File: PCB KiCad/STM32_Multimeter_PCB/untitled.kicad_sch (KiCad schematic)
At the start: 51 parts, among them J10 Conn_01x02_Pin, J6 Barrel_Jack, J7 Conn_01x02_Pin, J8 Barrel_Jack, J9 Barrel_Jack, Q1 NMOS, Q2 NMOS, Q3 NMOS, Q4 NMOS, Q5 NMOS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

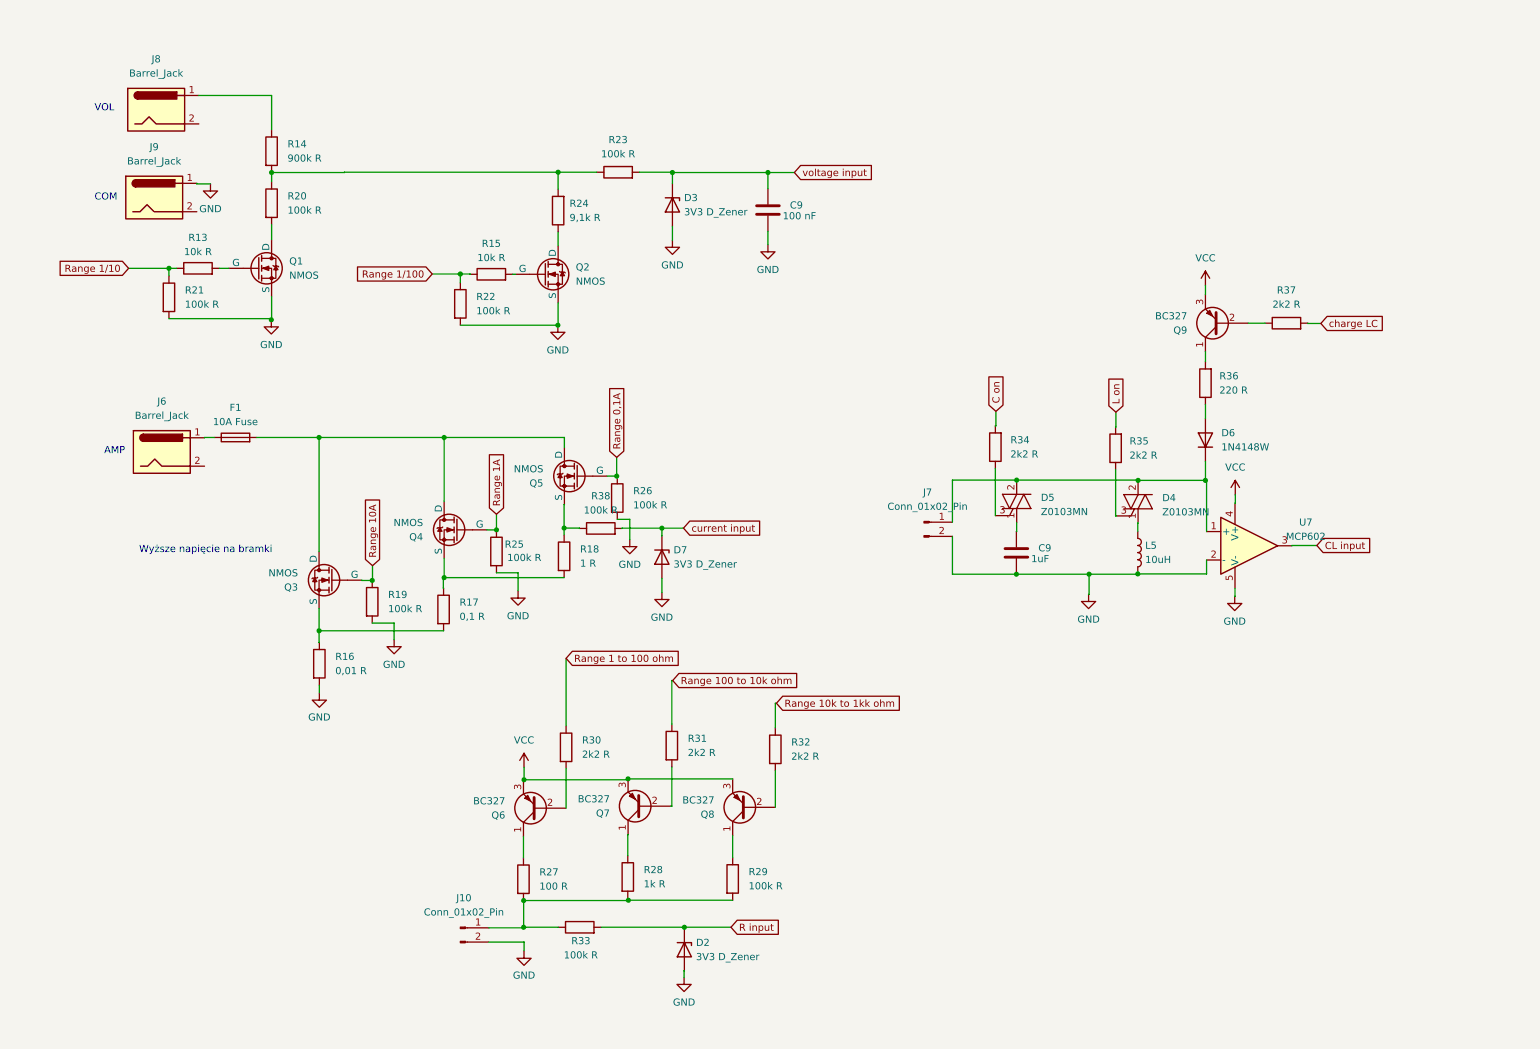
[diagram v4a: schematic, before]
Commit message: Added BJT for swiching range mosfets from 9V
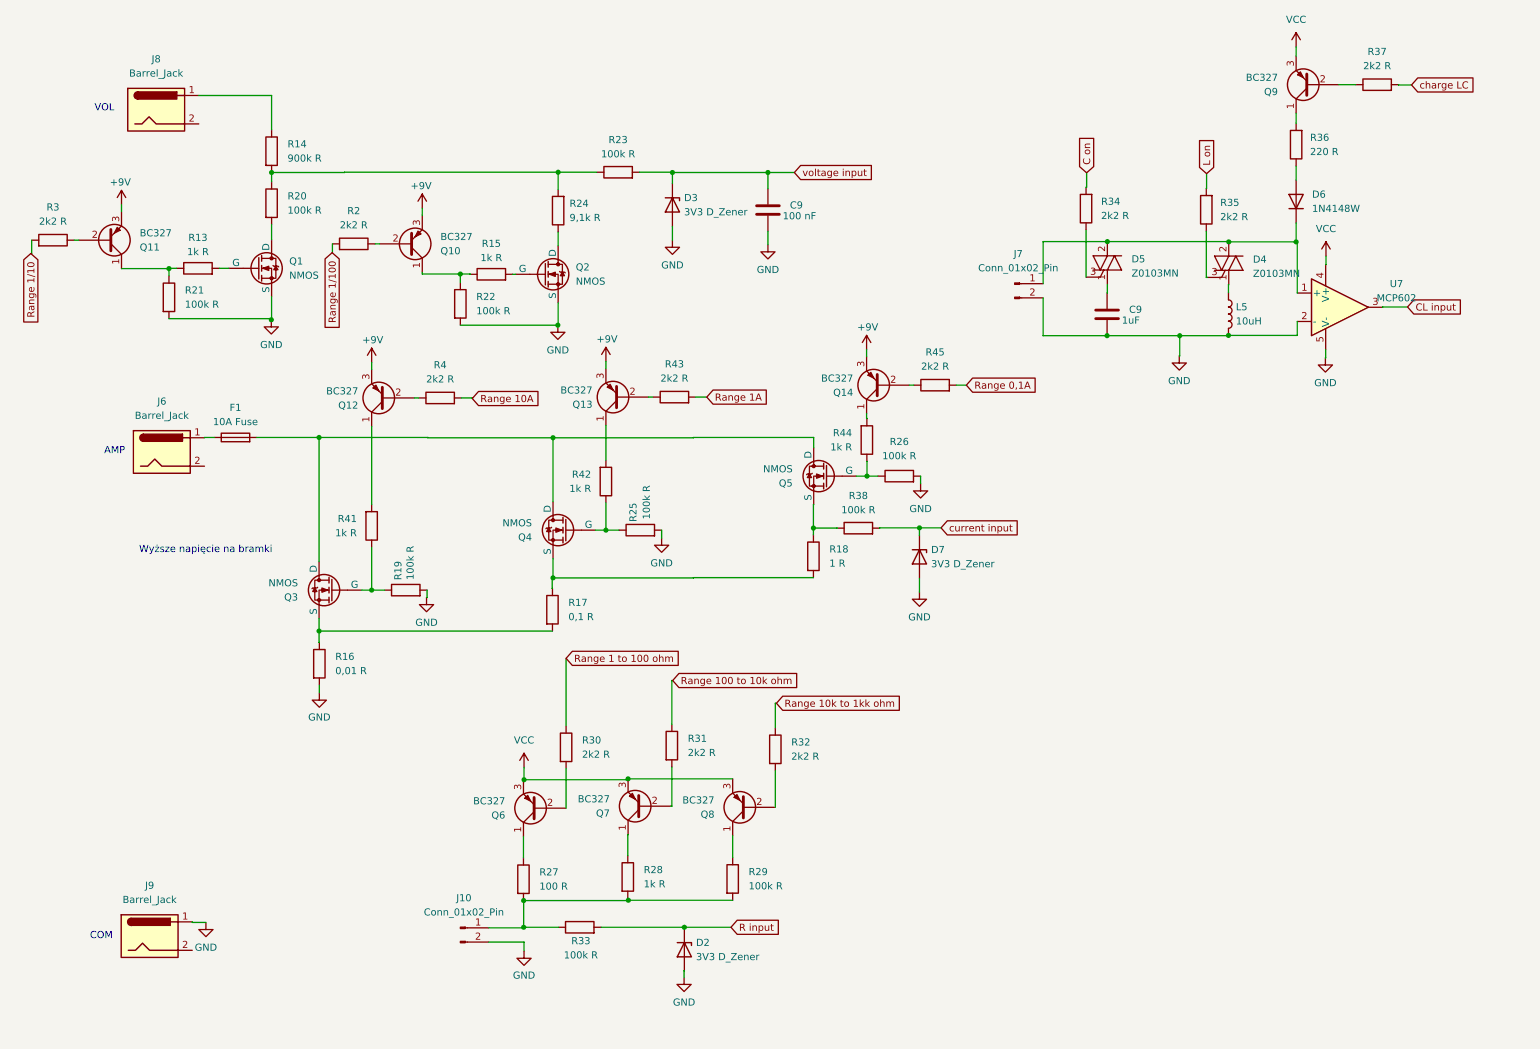
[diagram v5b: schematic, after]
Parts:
- added Q10, Q11, Q12, Q13, Q14: BC327, Package_TO_SOT_SMD:SOT-23-3, symbol Transistor_BJT:BC327
- added R2, R3, R4, R43, R45: 2k2 R, Resistor_SMD:R_0805_2012Metric, symbol Device:R
- added R41, R42, R44: 1k R, Resistor_SMD:R_0805_2012Metric, symbol Device:R
- R13, R15: value 10k R -> 1k R
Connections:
- net Range 0,1A: now also R45.2; no longer Q5.2 (G), R26.1
- net Range 10A: now also R4.2; no longer Q3.2 (G), R19.1
- net Range 1A: now also R43.2; no longer Q4.2 (G), R25.1
- net Range 1/10: now also R3.2; no longer R13.1, R21.1
- net Range 1/100: now also R2.2; no longer R15.1, R22.1
- new net: Q12.1 (C), R41.2
- new net: Q12.2 (B), R4.1
- new net: Q4.2 (G), R25.1, R42.1
- new net: Q11.1 (C), R13.1, R21.1
- new net: Q11.2 (B), R3.1
- new net: Q13.2 (B), R43.1
- new net: Q14.2 (B), R45.1
- new net: Q14.1 (C), R44.2
- new net: Q3.2 (G), R19.1, R41.1
- new net: Q13.1 (C), R42.2
- new net: Q10.1 (C), R15.1, R22.1
- new net: Q5.2 (G), R26.1, R44.1
- new net: Q10.2 (B), R2.1
- new net +9V: Q10.3 (E), Q11.3 (E), Q12.3 (E), Q13.3 (E), Q14.3 (E)
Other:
- moved on the sheet: C9, D4, D5, D6, D7, J7, J9, L5, Q3, Q4, Q5, Q9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

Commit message: Added shunt voltage amplifier
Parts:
- added R46: 43k R, Resistor_SMD:R_0805_2012Metric, symbol Device:R
- added R47: 330 R, Resistor_SMD:R_0805_2012Metric, symbol Device:R
- added R48: 390k R, Resistor_SMD:R_0805_2012Metric, symbol Device:R
- added U2: MCP602, symbol Simulation_SPICE:OPAMP
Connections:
- net GND: now also R46.1, U2.5 (V-)
- net VCC: now also U2.4 (V+)
- net current input: now also R48.2, U2.3; no longer D7.1 (K), R38.2
- new net: R47.2, R48.1, U2.2 (-)
- new net: R46.2, R47.1
- new net: D7.1 (K), R38.2, U2.1 (+)
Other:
- note added: "Gain=R1+R2)/R1= (390+43,33)/43,33= ~10"
- note removed: "Wyższe napięcie na bramki"

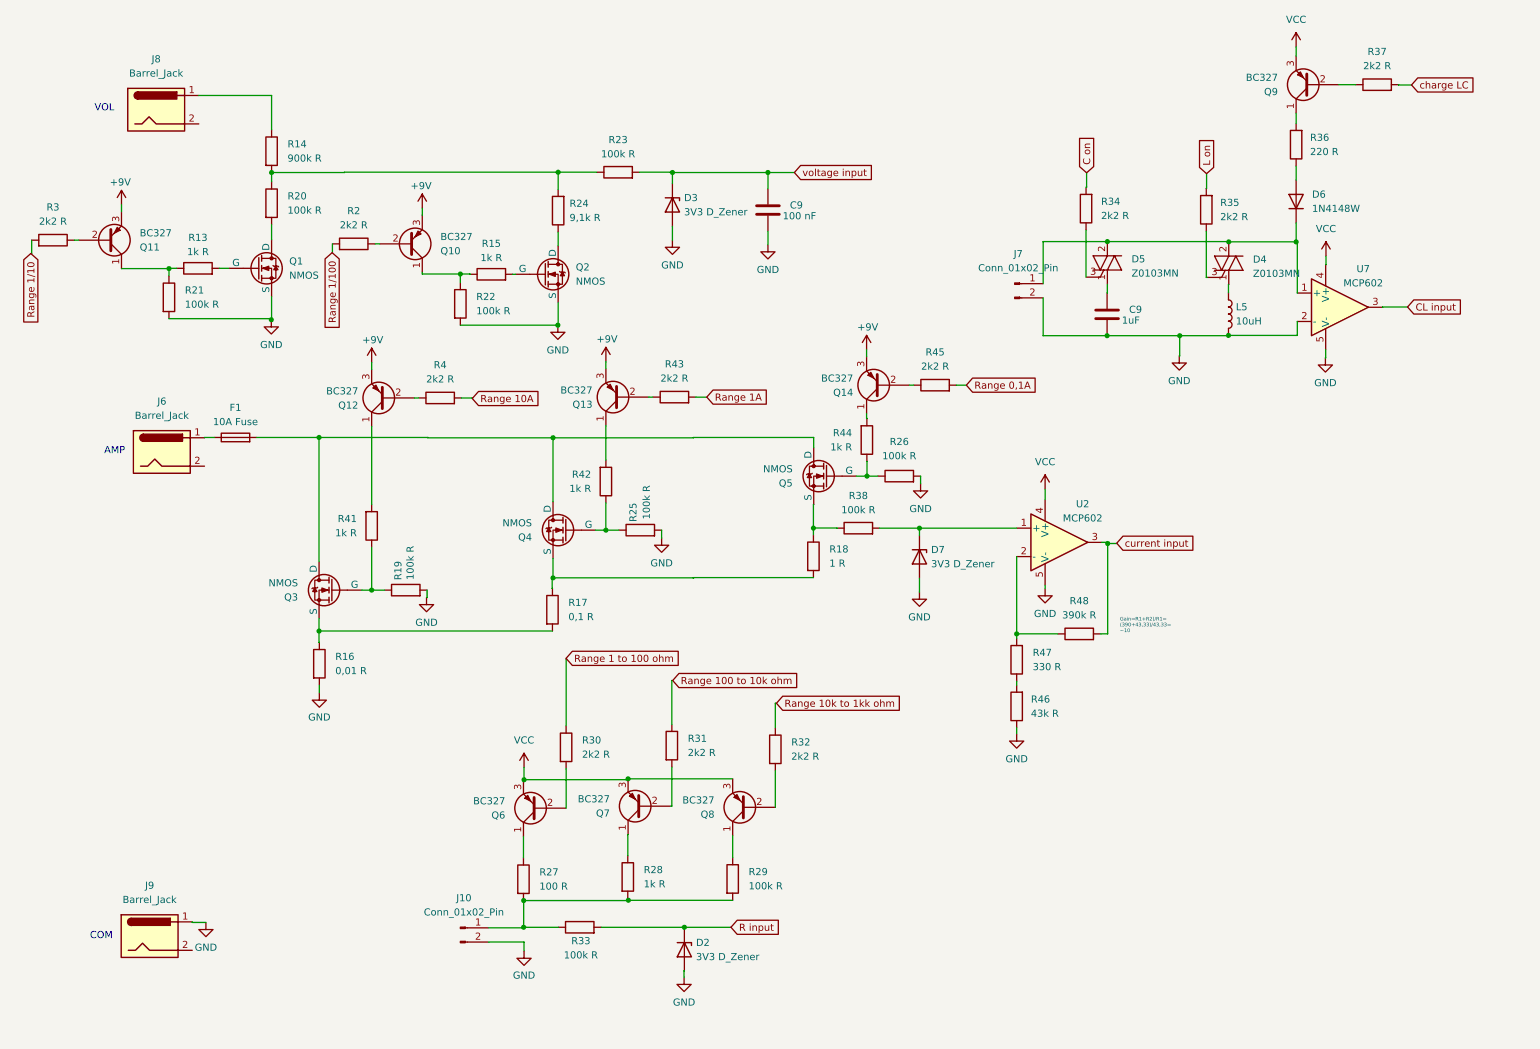
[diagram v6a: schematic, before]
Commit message: added resistance/voltage measurment relay
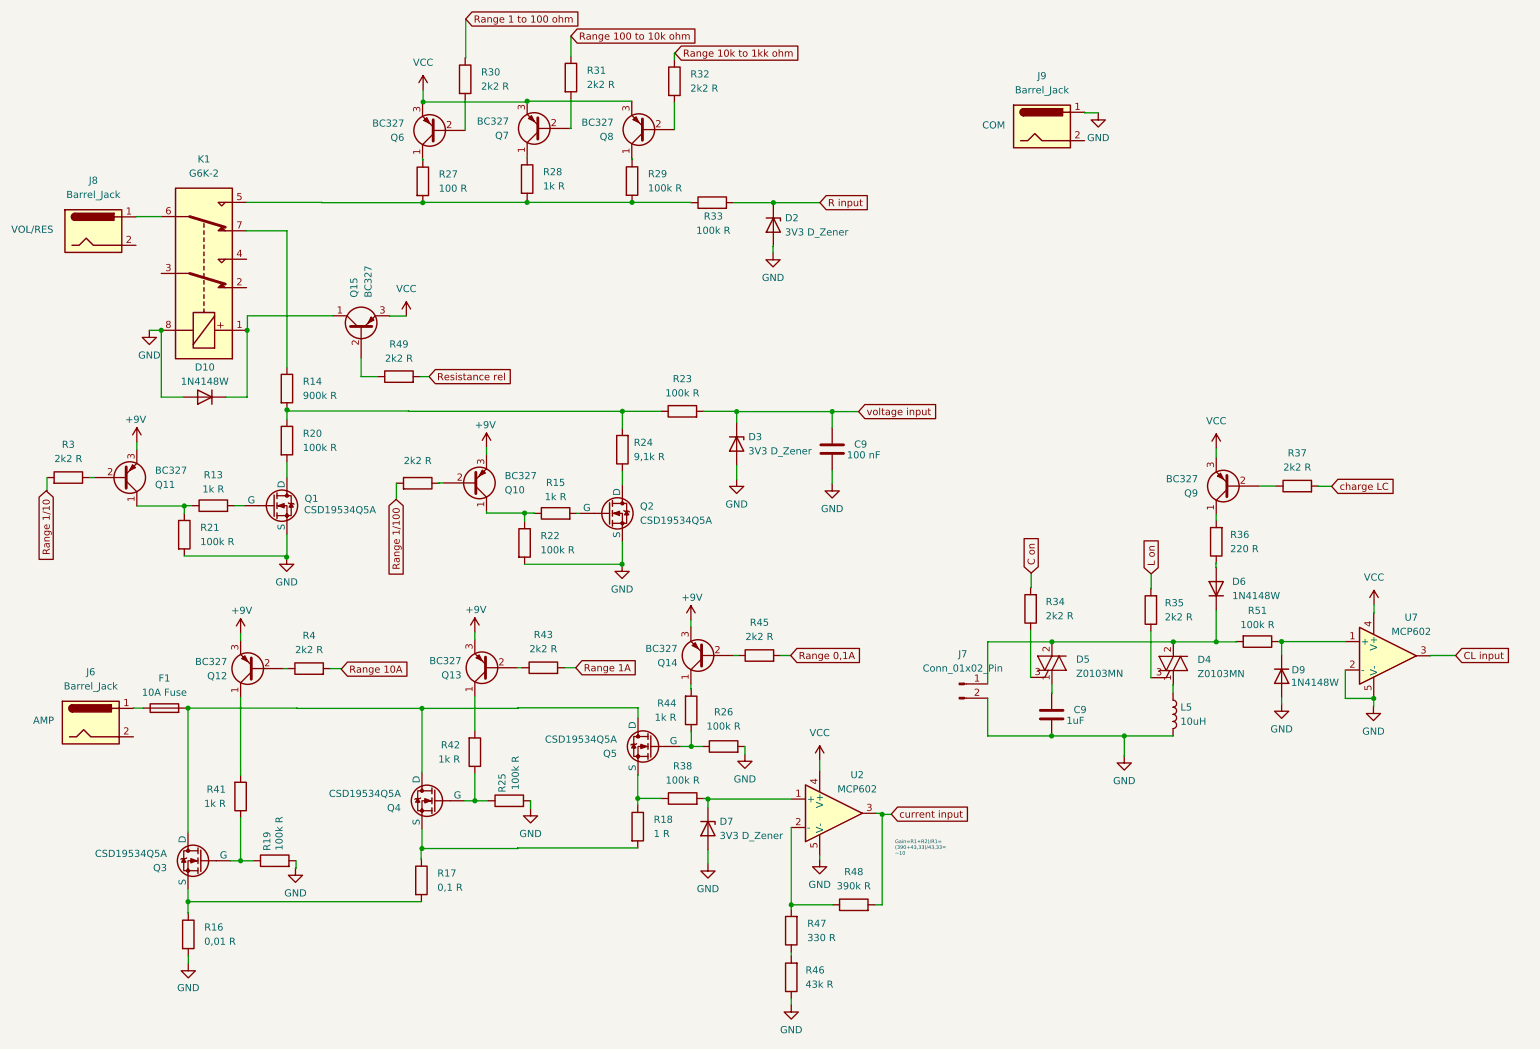
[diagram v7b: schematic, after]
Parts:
- removed J10: Conn_01x02_Pin, Connector_PinHeader_2.54mm:PinHeader_1x02_P2.54mm_Vertical, symbol Connector:Conn_01x02_Pin
- added D10, D9: 1N4148W, Diode_SMD:D_SOD-123, symbol Diode:1N4148W
- added K1: G6K-2, Relay_SMD:Relay_DPDT_Omron_G6K-2F-Y, symbol Relay:G6K-2
- added Q15: BC327, Package_TO_SOT_SMD:SOT-23-3, symbol Transistor_BJT:BC327
- added R49: 2k2 R, Resistor_SMD:R_0805_2012Metric, symbol Device:R
- added R51: 100k R, Resistor_SMD:R_0805_2012Metric, symbol Device:R
- Q1, Q2, Q3, Q4, Q5: value NMOS -> CSD19534Q5A; footprint (none) -> Package_DFN_QFN:PQFN-8-EP_6x5mm_P1.27mm_Generic
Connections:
- net GND: now also D10.2 (A), D9.2 (A), K1.8
- net VCC: now also Q15.3 (E)
- net at R14.1: now also K1.7; no longer J8.1
- net at D4.2 (A2), D4.4 (A4), D5.2 (A2)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: now also R51.2; no longer U7.1 (+)
- net at R27.2, R28.2, R29.2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: now also K1.5
- new net: D10.1 (K), K1.1, Q15.1 (C)
- new net: J8.1, K1.6
- new net: D9.1 (K), R51.1, U7.1 (+)
- new net: Q15.2 (B), R49.1
- new net Resistance rel: R49.2
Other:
- note added: "VOL/RES"
- note removed: "VOL"
- moved on the sheet: C9, D2, D3, D4, D5, D6, D7, F1, J6, J7, J8, J9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

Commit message: Added component footprints
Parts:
- F1: footprint (none) -> Fuse:Fuseholder_Clip-5x20mm_Eaton_1A5601-01_Inline_P20.80x6.76mm_D1.70mm_Horizontal
- J6, J8, J9: footprint (none) -> Connector_PinHeader_2.54mm:PinHeader_1x01_P2.54mm_Vertical
- L5: footprint (none) -> Inductor_SMD:L_Chilisin_BMRB00060650
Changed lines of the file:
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@@
       (effects (font (size 1.27 1.27)))
     )
-    (property "Footprint" "" (at 198.882 34.7472 0)
+    (property "Footprint" "Connector_PinHeader_2.54mm:PinHeader_1x01_P2.54mm_Vertical" (at 198.882 34.7472 0)
       (effects (font (size 1.27 1.27)) hide)
     )
@@
       (effects (font (size 1.27 1.27)))
     )
-    (property "Footprint" "" (at 29.3624 53.4416 0)
+    (property "Footprint" "Connector_PinHeader_2.54mm:PinHeader_1x01_P2.54mm_Vertical" (at 29.3624 53.4416 0)
       (effects (font (size 1.27 1.27)) hide)
     )
@@
       (effects (font (size 1.27 1.27)) (justify left))
     )
-    (property "Footprint" "" (at 221.0308 138.7856 0)
+    (property "Footprint" "Inductor_SMD:L_Chilisin_BMRB00060650" (at 221.0308 138.7856 0)
       (effects (font (size 1.27 1.27)) hide)
     )
@@
       (effects (font (size 1.27 1.27)))
     )
-    (property "Footprint" "" (at 40.7924 139.446 90)
+    (property "Footprint" "Fuse:Fuseholder_Clip-5x20mm_Eaton_1A5601-01_Inline_P20.80x6.76mm_D1.70mm_Horizontal" (at 40.7924 139.446 90)
       (effects (font (size 1.27 1.27)) hide)
     )
@@
       (effects (font (size 1.27 1.27)))
     )
-    (property "Footprint" "" (at 28.9052 141.2748 0)
-      (effects (font (size 1.27 1.27)) hide)
-    )
+    (property "Footprint" "Connector_PinHeader_2.54mm:PinHeader_1x01_P2.54mm_Vertical" (at 28.9052 141.2748 0)
+      (effects (font (size 1.27 1.27)) hide)
+    )
